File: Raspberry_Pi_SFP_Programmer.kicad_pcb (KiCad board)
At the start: 2 copper layers, 65 x 56 mm, 18 parts, among them J1 RPi_GPIO, J2 SFP+, J4 Conn_02x03_Odd_Even, Q1 BC847, Q2 BC847

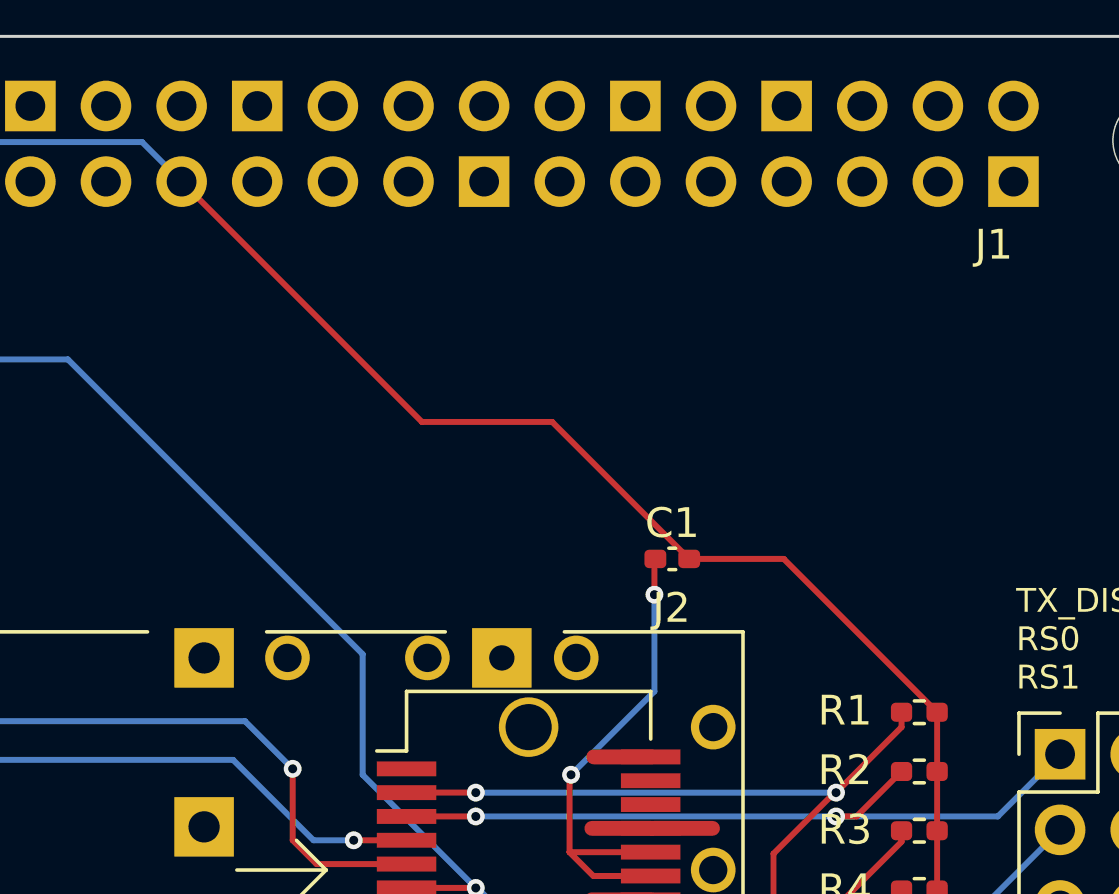
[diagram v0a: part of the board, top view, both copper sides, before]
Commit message: Fix PSU cap
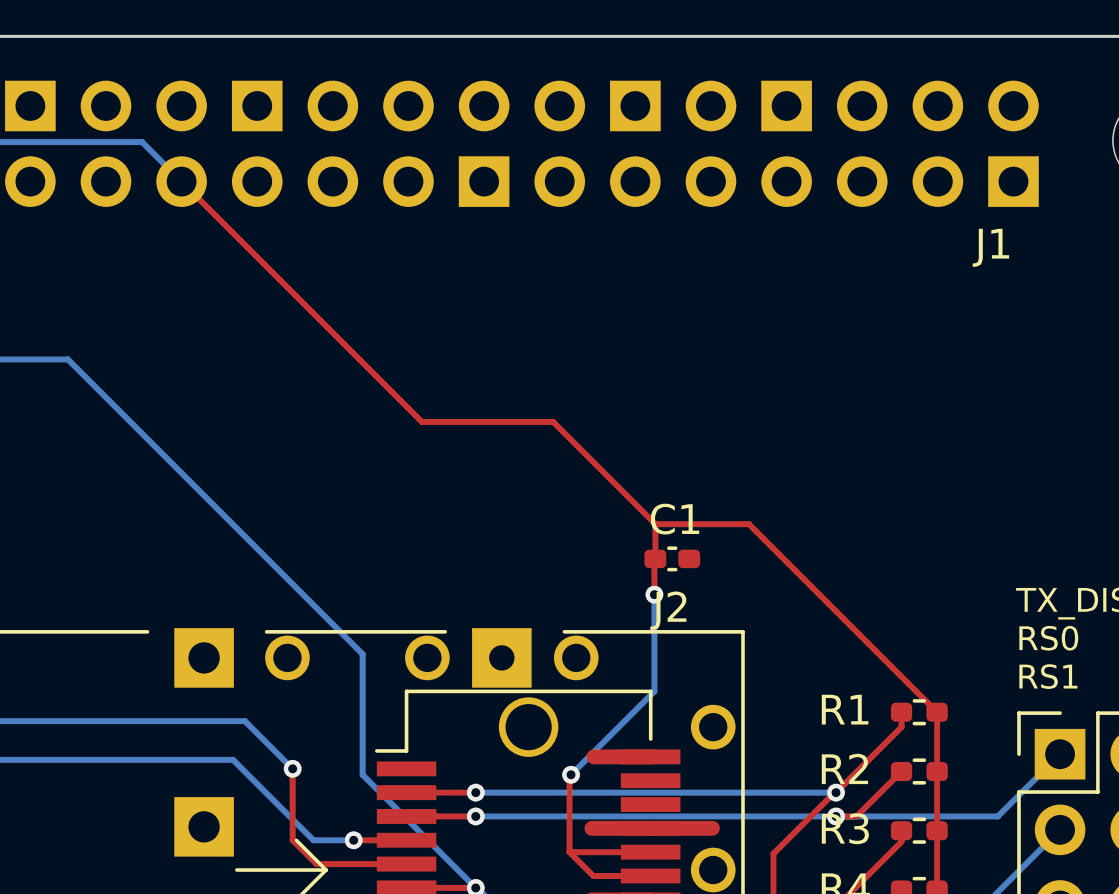
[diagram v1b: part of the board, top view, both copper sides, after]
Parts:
- turned C1 to 0 degrees
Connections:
- C1 pad 2: Net-(J2-VccR) -> GND
- J2 pad 15: Net-(J2-VccR) -> +3.3V
- J2 pad 16: Net-(J2-VccR) -> +3.3V
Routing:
- net +3.3V: track 87.6 -> 105.6 mm, vias 0 -> 2
- net Net-(J2-VccR): track 16.8 -> 0.00 mm, vias 2 -> 0
